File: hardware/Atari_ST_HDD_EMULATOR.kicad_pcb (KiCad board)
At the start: 2 copper layers, 53 x 73 mm, 33 parts, among them J1 DB25_Male, J2 473092285, J3 473092285, J4 ID Select, J5 RTC Enable, J7 IDC 20pin, SW1 PICO RESET, U2 TXB0108PWR, U3 TXB0108PWR, U4 74HCT125PW, U5 74HCT85PW, U6 Pico

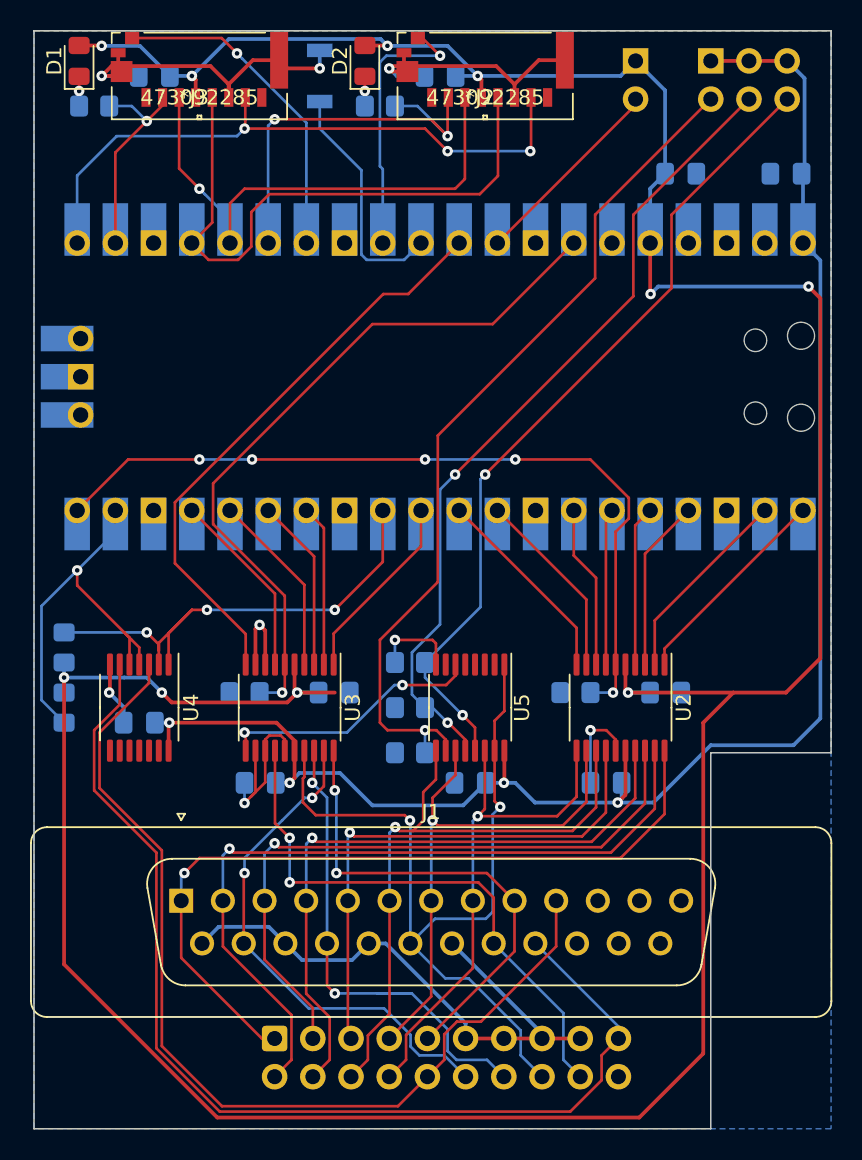
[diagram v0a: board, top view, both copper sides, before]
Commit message: Changed schematic to reflect different pinout of PWR package on the TX0108. PCB design needs changing
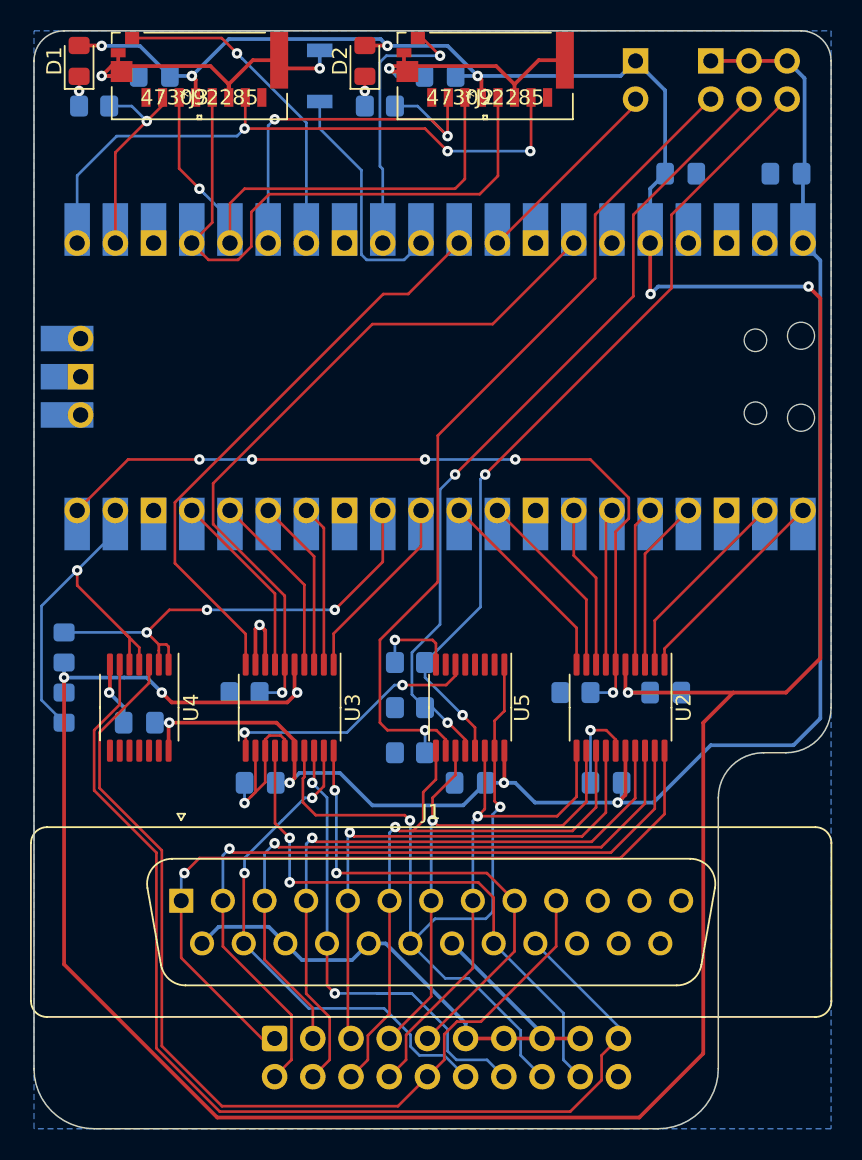
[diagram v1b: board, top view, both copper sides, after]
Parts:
- removed C10: 100nF, Capacitor_SMD:C_0805_2012Metric_Pad1.18x1.45mm_HandSolder
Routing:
- net +3V3: track 232.6 -> 228.7 mm
- net IRQ: track 33.3 -> 30.9 mm
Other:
- outline, holes or cut-outs redrawn

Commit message: Started work on simplified version with alternative level shifters
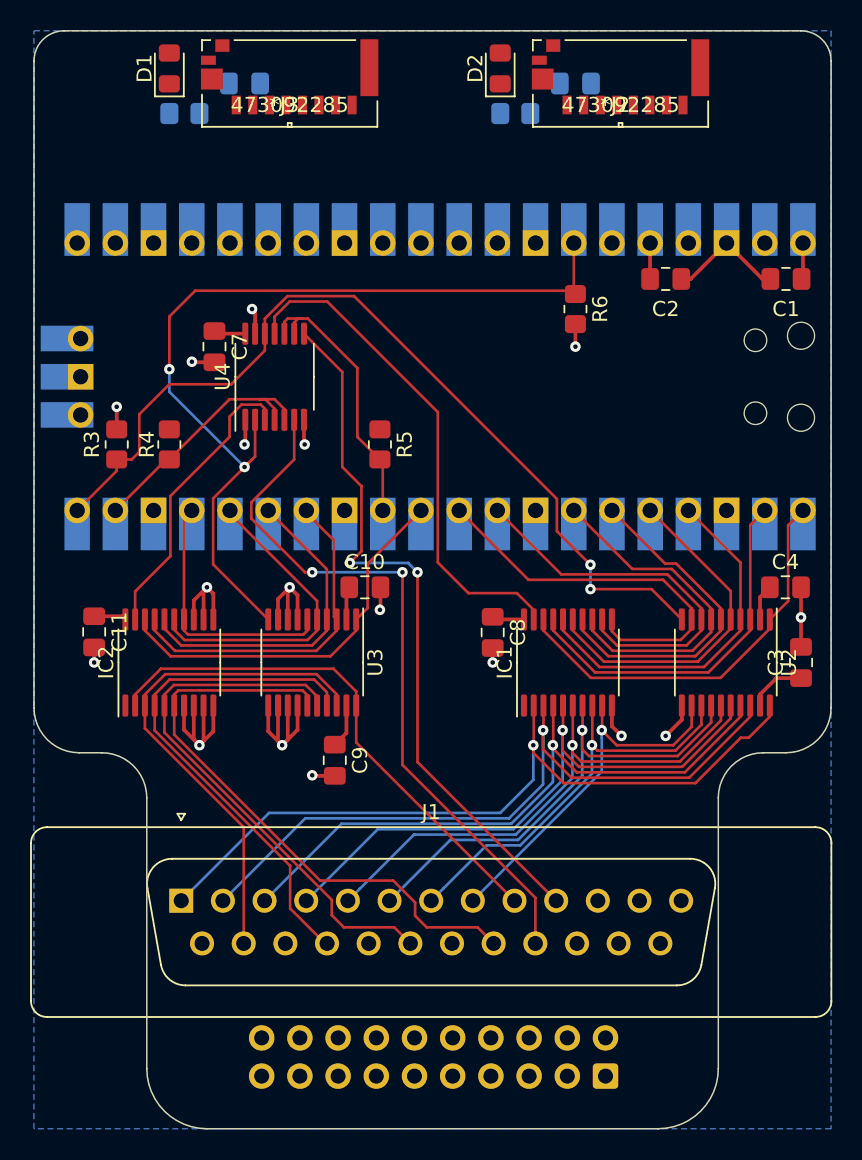
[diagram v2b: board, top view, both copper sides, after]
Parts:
- removed the C1 at (178.0, 59.5)
- removed J4: ID Select, Connector_PinHeader_2.54mm:PinHeader_2x03_P2.54mm_Vertical
- removed J5: RTC Enable, Connector_PinHeader_2.54mm:PinHeader_1x02_P2.54mm_Vertical
- removed R16, R17, R18: R10K, Resistor_SMD:R_0805_2012Metric_Pad1.20x1.40mm_HandSolder
- removed SW1: PICO RESET, Button_Switch_SMD:SW_SPST_B3U-1000P
- removed U5: 74HCT85PW, Package_SO:TSSOP-16_4.4x5mm_P0.65mm
- added C10: 100nF, Capacitor_SMD:C_0805_2012Metric_Pad1.18x1.45mm_HandSolder, F.Cu at (150.0, 87.0)
- added C11: 100nF, Capacitor_SMD:C_0805_2012Metric_Pad1.18x1.45mm_HandSolder, F.Cu at (132.0, 90.0)
- added C3: 100nF, Capacitor_SMD:C_0805_2012Metric_Pad1.18x1.45mm_HandSolder, F.Cu at (179.0, 92.0)
- added IC1: SN74CB3T3245PWR, Package_SO:TSSOP-20_4.4x6.5mm_P0.65mm, F.Cu at (163.5, 92.0)
- added IC2: SN74CB3T3245PWR, Package_SO:TSSOP-20_4.4x6.5mm_P0.65mm, F.Cu at (137.0, 92.0)
- C1: renamed from C2; moved to F.Cu
- C2: renamed from C3; moved to F.Cu
- C4, C7, C8, C9: moved to F.Cu
- R3, R4, R5, R6: value R1K -> R10K; moved to F.Cu
- moved C1 35.6 mm to (178.0, 66.5)
- moved R3 34.7 mm to (133.5, 77.5), turned to 90 degrees
- moved R6 33.7 mm to (164.0, 68.5), turned to 270 degrees
- moved C7 25.5 mm to (140.0, 71.0), turned to 270 degrees
- moved R5 25.0 mm to (151.0, 77.5), turned to 270 degrees
- moved U4 23.8 mm to (144.0, 73.0), turned to 90 degrees
- moved J7 22.1 mm to (166.0, 119.5), turned to 90 degrees
- moved R4 18.8 mm to (137.0, 77.5)
- moved C4 10.6 mm to (178.0, 87.0)
- moved C8 10.1 mm to (158.5, 90.0), turned to 270 degrees
- moved C5 9.01 mm to (164.0, 53.5)
- moved D2 9.01 mm to (159.0, 52.5)
- moved J2 9.01 mm to (167.0, 53.5)
- moved R2 9.01 mm to (160.0, 55.5)
- moved U2 7.62 mm to (174.0, 92.0)
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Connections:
- C8 pad 1: +5V -> +3V3
- U2 pad 10: /D7 -> DATABUSENABLE
- U2 pad 11: AD7 -> GND
- U2 pad 12: AD6 -> AD7
- U2 pad 13: AD5 -> AD6
- U2 pad 14: /AD4 -> AD5
- U2 pad 15: GND -> /AD4
- U2 pad 16: +5V -> /AD3
- U2 pad 17: /AD3 -> /AD2
- U2 pad 18: /AD2 -> /AD1
- U2 pad 19: /AD1 -> +5V
- U2 pad 2: /D1 -> +3V3
- U2 pad 3: /D2 -> /D1
- U2 pad 4: /D3 -> /D2
- U2 pad 5: +3V3 -> /D3
- U2 pad 6: DATABUSENABLE -> /D4
- U2 pad 7: /D4 -> /D5
- U2 pad 8: /D5 -> /D6
- U2 pad 9: /D6 -> /D7
- U3 pad 10: SELECTED -> CNTRLBUSENABLE
- U3 pad 11: CONTROLLERID -> GND
- U3 pad 14: ARW -> GND
- U3 pad 15: GND -> ARW
- U3 pad 16: +5V -> AA1
- U3 pad 17: AA1 -> AACK
- U3 pad 18: AACK -> ARST
- U3 pad 19: ARST -> +5V
- U3 pad 2: RST -> +3V3
- U3 pad 3: ACK -> RST
- U3 pad 4: A1 -> ACK
- U3 pad 5: +3V3 -> A1
- U3 pad 6: CNTRLBUSENABLE -> RW
- U3 pad 7: RW -> GND
- U4 pad 1: IRQ -> GND
- U4 pad 10: (no net) -> IRQ
- U4 pad 11: (no net) -> /~DATABUSENABLE
- U4 pad 12: (no net) -> DATABUSENABLE
- U4 pad 13: (no net) -> GND
- U4 pad 2: IRQ -> CNTRLBUSENABLE
- U4 pad 3: AIRQ -> /~CNTRLBUSENABLE
- U4 pad 8: (no net) -> AIRQ
- U4 pad 9: (no net) -> IRQ
- U6 pad 30: PICO_RST -> Net-(U6-Pad30)
- U6 pad 31: SELECTED -> Net-(U6-Pad31)
- U6 pad 32: RTC_ENABLE -> Net-(U6-Pad32)
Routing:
- net +3V3: track 228.7 -> 11.3 mm, vias 10 -> 0
- net +5V: track 113.1 -> 11.4 mm, vias 4 -> 0
- net Net-(J4-Pad2): track 57.7 -> 0.00 mm, vias 1 -> 0
- net Net-(J4-Pad6): track 54.7 -> 0.00 mm, vias 2 -> 0
- net Net-(J4-Pad4): track 54.4 -> 0.00 mm, vias 2 -> 0
- net GND: track 115.6 -> 68.5 mm, vias 8 -> 17
- net SPI_RX: track 42.2 -> 0.00 mm, vias 3 -> 0
- net SPI_CLK: track 39.9 -> 0.00 mm
- net SELECTED: track 38.8 -> 0.00 mm
- net SPI_TX: track 35.4 -> 0.00 mm, vias 1 -> 0
- net /~DATABUSENABLE: track 0.00 -> 33.8 mm
- net CS1: track 27.3 -> 0.00 mm, vias 2 -> 0
- net ADRQ: track 72.0 -> 47.6 mm, vias 0 -> 2
- net CD0: track 21.9 -> 0.00 mm, vias 1 -> 0
- net /~CNTRLBUSENABLE: track 0.00 -> 19.6 mm
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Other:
- outline, holes or cut-outs redrawn

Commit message: Initial tracing complete -- awaiting wiring of the IDC connector
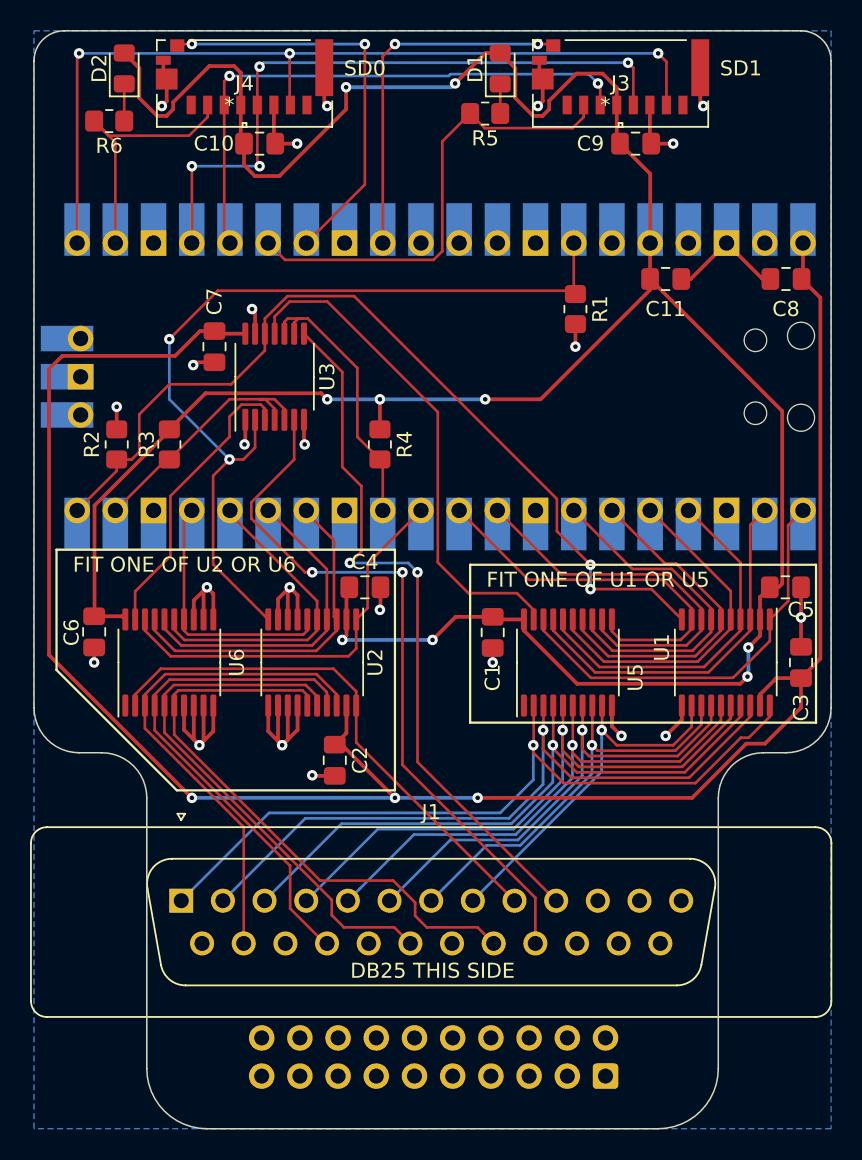
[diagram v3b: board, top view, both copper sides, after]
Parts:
- removed the D2 at (159.0, 52.5)
- removed the R2 at (160.0, 55.5)
- added D1: LED, LED_SMD:LED_0805_2012Metric_Pad1.15x1.40mm_HandSolder, F.Cu at (159.0, 52.5)
- added R5: R220, Resistor_SMD:R_0805_2012Metric_Pad1.20x1.40mm_HandSolder, F.Cu at (158.0, 55.5)
- C10: renamed from C6; moved to F.Cu
- C9: renamed from C5; moved to F.Cu
- R6: renamed from R1; moved to F.Cu
- moved C9 5.66 mm to (168.0, 57.5), turned to 0 degrees
- moved R6 5.02 mm to (133.0, 56.0), turned to 180 degrees
- moved C10 4.12 mm to (143.0, 57.5), turned to 0 degrees
- moved D2 3.00 mm to (134.0, 52.5)
- moved J4 3.00 mm to (142.0, 53.5)
- renumbered C8 to C1, C2 to C11, C9 to C2, C10 to C4, C4 to C5, C11 to C6, C1 to C8, D1 to D2, J7 to J2, J2 to J3, J3 to J4, R6 to R1, R3 to R2, R4 to R3, R5 to R4, U2 to U1, U3 to U2, U4 to U3, U6 to U4, IC1 to U5, IC2 to U6
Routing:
- net +3V3: track 11.3 -> 187.1 mm, vias 0 -> 9
- net +5V: track 11.4 -> 133.9 mm, vias 0 -> 3
- net SPI_RX: track 0.00 -> 58.3 mm, vias 0 -> 3
- net SPI_CLK: track 0.00 -> 43.9 mm, vias 0 -> 4
- net SPI_TX: track 0.00 -> 37.7 mm, vias 0 -> 2
- net CS1: track 0.00 -> 31.3 mm
- net CD0: track 0.00 -> 27.4 mm, vias 0 -> 2
- net CD1: track 0.00 -> 24.1 mm, vias 0 -> 2
- net GND: track 68.5 -> 88.4 mm, vias 17 -> 23
- net CS0: track 0.00 -> 18.0 mm
- net Net-(D2-Pad1): track 0.00 -> 2.48 mm
- net Net-(D1-Pad1): track 0.00 -> 1.98 mm
- net CNTRLBUSENABLE: track 60.0 -> 58.0 mm
- net CS: track 26.0 -> 26.7 mm
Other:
- board text added: "DB25 THIS SIDE"
- board text added: "FIT ONE OF U1 OR U5"
- board text added: "FIT ONE OF U2 OR U6"
- board text added: "IDC THIS SIDE"
- board text added: "PICO THIS SIDE"
- board text added: "SD0"
- board text added: "SD1"

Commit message: First draft of v1.0_dh219
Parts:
- moved J2 23.2 mm to (143.0, 116.5), turned to 270 degrees
- moved C4 4.74 mm to (151.5, 91.5), turned to 270 degrees
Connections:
- J2 pad 10: AIRQ -> GND
- J2 pad 11: GND -> AD5
- J2 pad 12: ARST -> AA1
- J2 pad 13: GND -> AD6
- J2 pad 14: AACK -> GND
- J2 pad 15: GND -> AD7
- J2 pad 16: AA1 -> ARW
- J2 pad 17: GND -> ACS
- J2 pad 18: ARW -> ADRQ
- J2 pad 19: ADRQ -> AIRQ
- J2 pad 2: /AD1 -> GND
- J2 pad 3: /AD2 -> /AD1
- J2 pad 4: /AD3 -> ARST
- J2 pad 5: /AD4 -> /AD2
- J2 pad 6: AD5 -> GND
- J2 pad 7: AD6 -> /AD3
- J2 pad 8: AD7 -> AACK
- J2 pad 9: ACS -> /AD4
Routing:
- net ARST: track 33.9 -> 44.9 mm
- net AD7: track 24.8 -> 35.8 mm
- net /AD0: track 51.3 -> 62.1 mm
- net /AD1: track 48.0 -> 58.7 mm
- net /AD4: track 35.9 -> 46.6 mm
- net /AD2: track 43.2 -> 53.8 mm
- net /AD3: track 40.5 -> 51.1 mm
- net AD5: track 33.0 -> 43.5 mm
- net AD6: track 28.5 -> 38.8 mm
- net ACS: track 35.0 -> 45.1 mm
- net AACK: track 34.5 -> 44.1 mm
- net ARW: track 40.0 -> 49.5 mm
- net AIRQ: track 47.6 -> 56.9 mm
- net ADRQ: track 47.6 -> 57.0 mm
- net AA1: track 36.6 -> 45.7 mm
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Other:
- board text added: "v1.0_DH219 Board design Copyright 2023 D Henderson Product design by S Bradford github.com/dh219 github.com/gotaproblem"
- board text added: "~RPP HDD EMU"

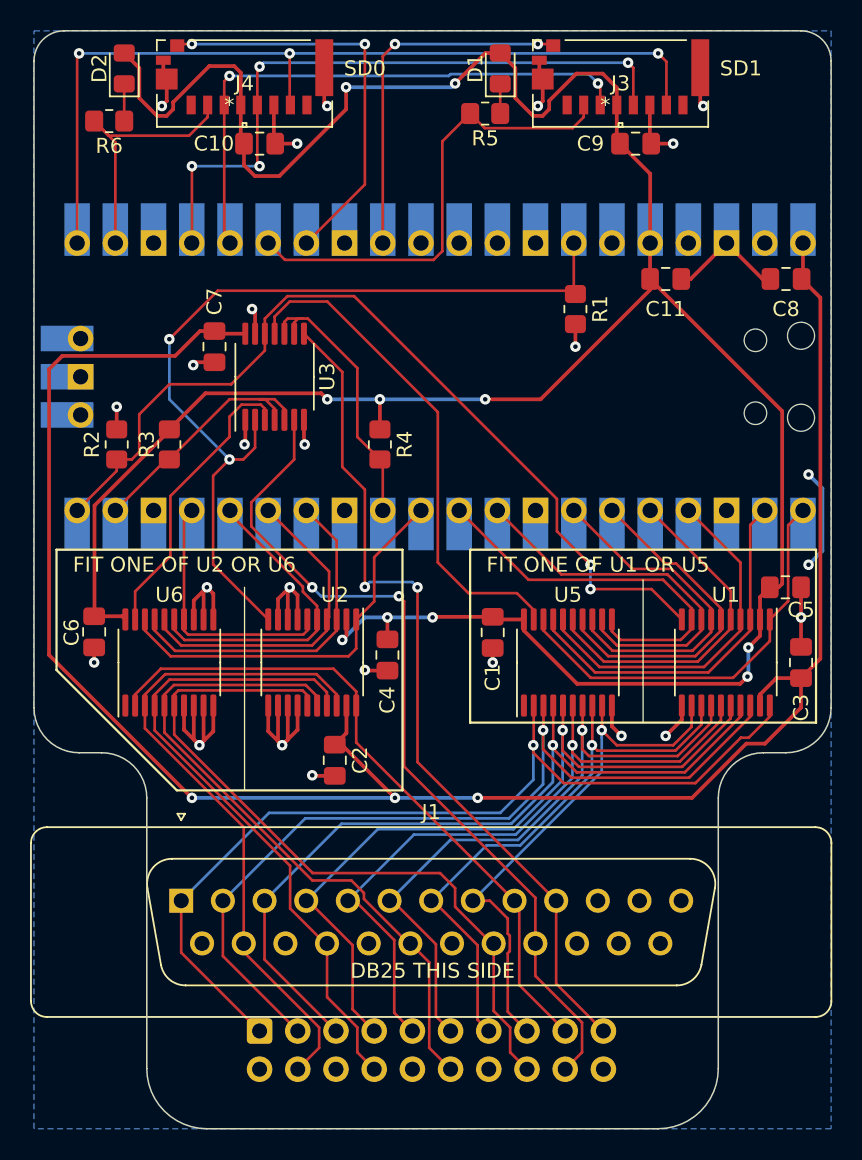
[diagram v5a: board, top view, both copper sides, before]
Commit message: Fixing some issues with 1.0 => no logic inversion for the Texas chips & changing the 125 supply voltage to 3V3.
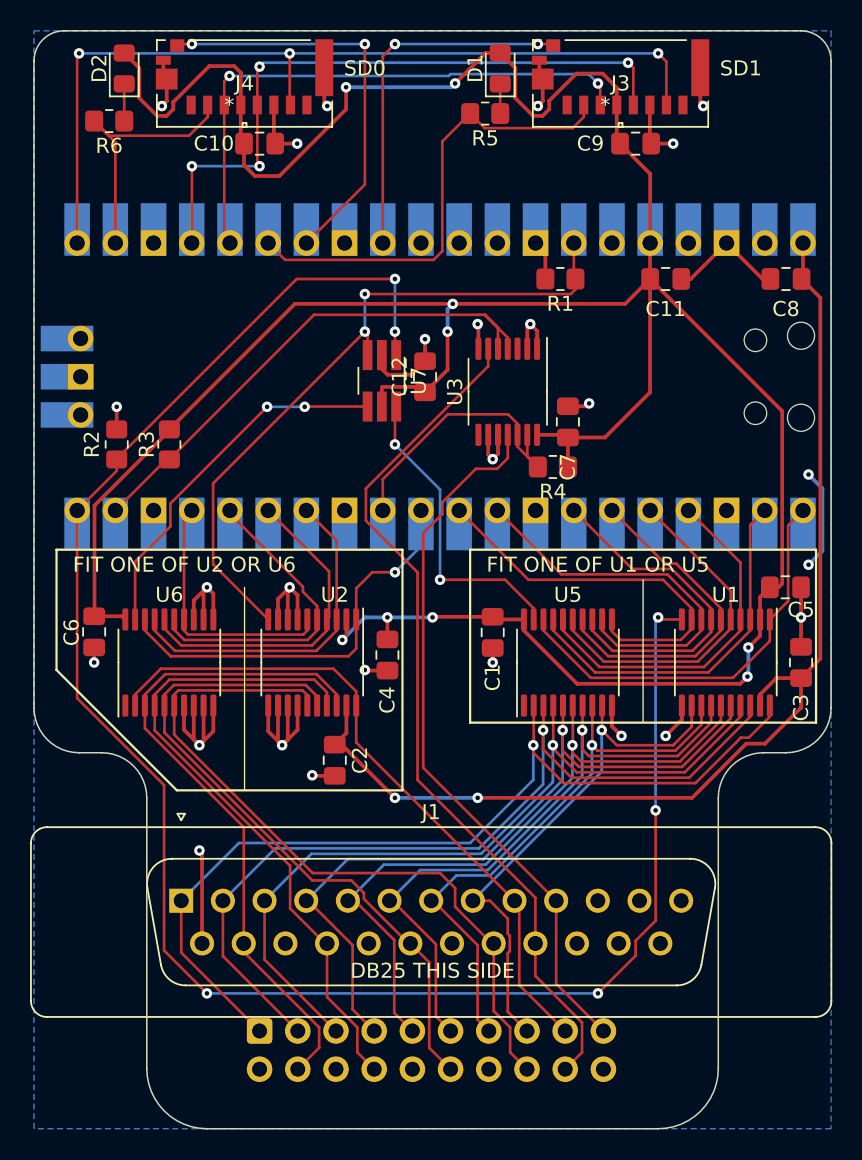
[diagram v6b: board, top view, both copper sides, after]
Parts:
- added C12: 100nF, Capacitor_SMD:C_0805_2012Metric_Pad1.18x1.45mm_HandSolder, F.Cu at (154.0, 73.0)
- added U7: 74LVC2G04, Package_TO_SOT_SMD:TSOT-23-6_HandSoldering, F.Cu at (151.1, 73.3)
- moved C7 24.0 mm to (163.5, 76.0), turned to 90 degrees
- moved U3 15.5 mm to (159.5, 74.0), turned to 270 degrees
- moved R4 11.6 mm to (162.5, 79.0), turned to 180 degrees
- moved R1 2.24 mm to (163.0, 66.5), turned to 180 degrees
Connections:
- C7 pad 1: +5V -> +3V3
- U3 pad 10: IRQ -> GND
- U3 pad 11: /~DATABUSENABLE -> AIRQ
- U3 pad 12: DATABUSENABLE -> IRQ
- U3 pad 13: GND -> IRQ
- U3 pad 14: +5V -> +3V3
- U3 pad 2: CNTRLBUSENABLE -> GND
- U3 pad 3: /~CNTRLBUSENABLE -> Net-(U3-Pad3)
- U3 pad 8: AIRQ -> Net-(U3-Pad8)
- U3 pad 9: IRQ -> GND
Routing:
- net DATABUSENABLE: track 60.4 -> 123.0 mm, vias 2 -> 6
- net +5V: track 133.9 -> 73.8 mm, vias 3 -> 2
- net +3V3: track 186.4 -> 212.9 mm, vias 10 -> 9
- net DRQ: track 17.3 -> 35.5 mm
- net GND: track 95.1 -> 112.0 mm, vias 25 -> 26
- net /~DATABUSENABLE: track 33.8 -> 21.2 mm, vias 0 -> 2
- net CNTRLBUSENABLE: track 58.0 -> 46.2 mm
- net AIRQ: track 56.9 -> 47.8 mm, vias 2 -> 0
- net /~CNTRLBUSENABLE: track 19.6 -> 24.5 mm, vias 0 -> 2
- net CS: track 26.7 -> 27.6 mm, vias 0 -> 1
- net ADRQ: track 57.0 -> 57.7 mm, vias 2 -> 0
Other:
- board text added: "v1.1_DH219 Board design Copyright 2023 D Henderson Product design by S Bradford github.com/dh219 github.com/gotaproblem"
- board text removed: "v1.0_DH219 Board design Copyright 2023 D Henderson Product design by S Bradford github.com/dh219 github.com/gotaproblem"
